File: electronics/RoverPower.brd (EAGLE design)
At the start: 31.8 x 31.8 mm, 13 parts, among them U1 LM2940

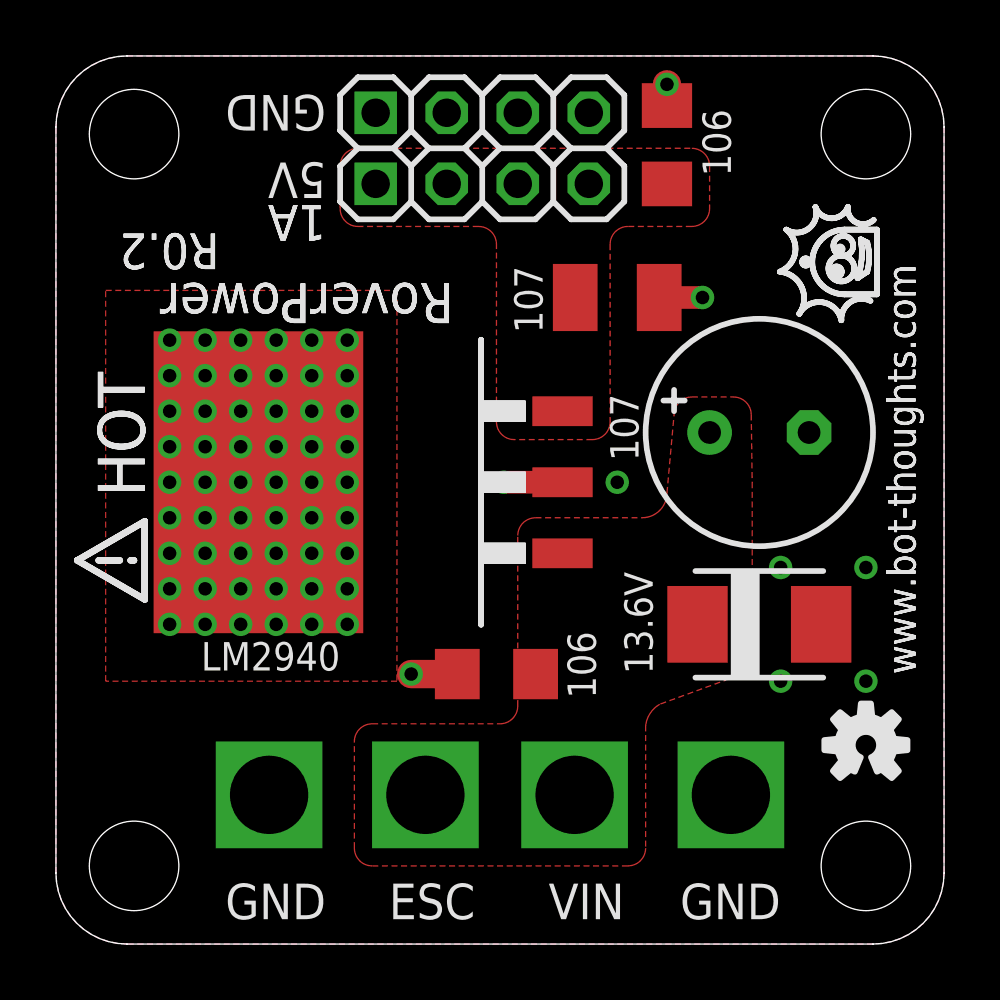
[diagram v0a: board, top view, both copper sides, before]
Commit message: copied power polygons to bottom layer, added vias. Changed capacitor to smaller version, revised TVS to higher voltage, changed layout.
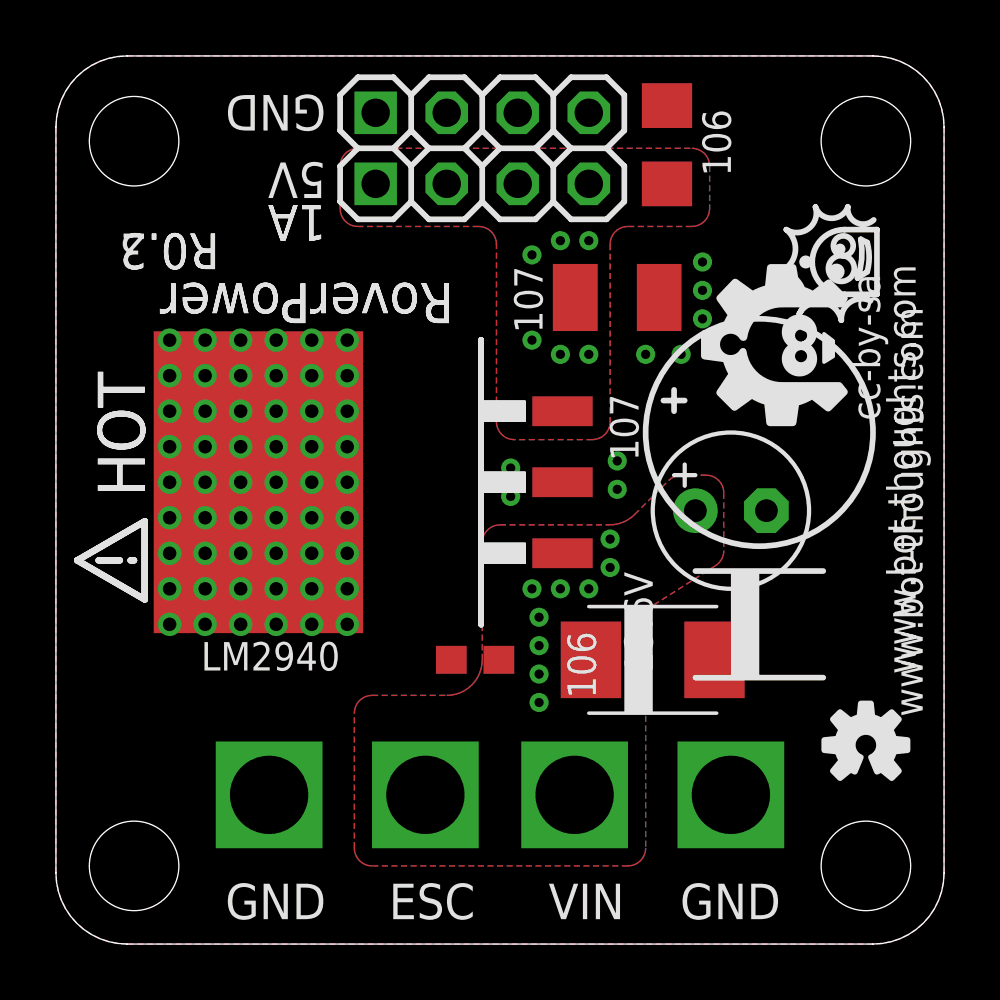
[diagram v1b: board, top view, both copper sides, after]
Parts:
- removed LOGO1: OSHW-LOGOS, SparkFun-Aesthetics:OSHW-LOGO-S
- added U$2: BTLOGO-LOGO-MD, bt:BTLOGOM
- C1: value 107 -> 476; device rcl:E3,5-8 -> rcl:E2,5-6
- C2: value 106 -> 104; device rcl:C1206 -> rcl:C0603
- D1: value 13.6V -> 25.5V
- moved D1 4.02 mm to (21.3, 10.2)
- moved C1 2.97 mm to (24.1, 15.5)
- moved C2 0.92 mm to (15.0, 10.2)
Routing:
- net GND: track 6.06 -> 0.00 mm
- added copper zone on layer 16, net 5V
- added copper zone on layer 16, net BAT+
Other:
- board text added: "R0.3"
- board text added: "cc-by-sa"

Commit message: Added more vias, changed output 10uf to .1uf
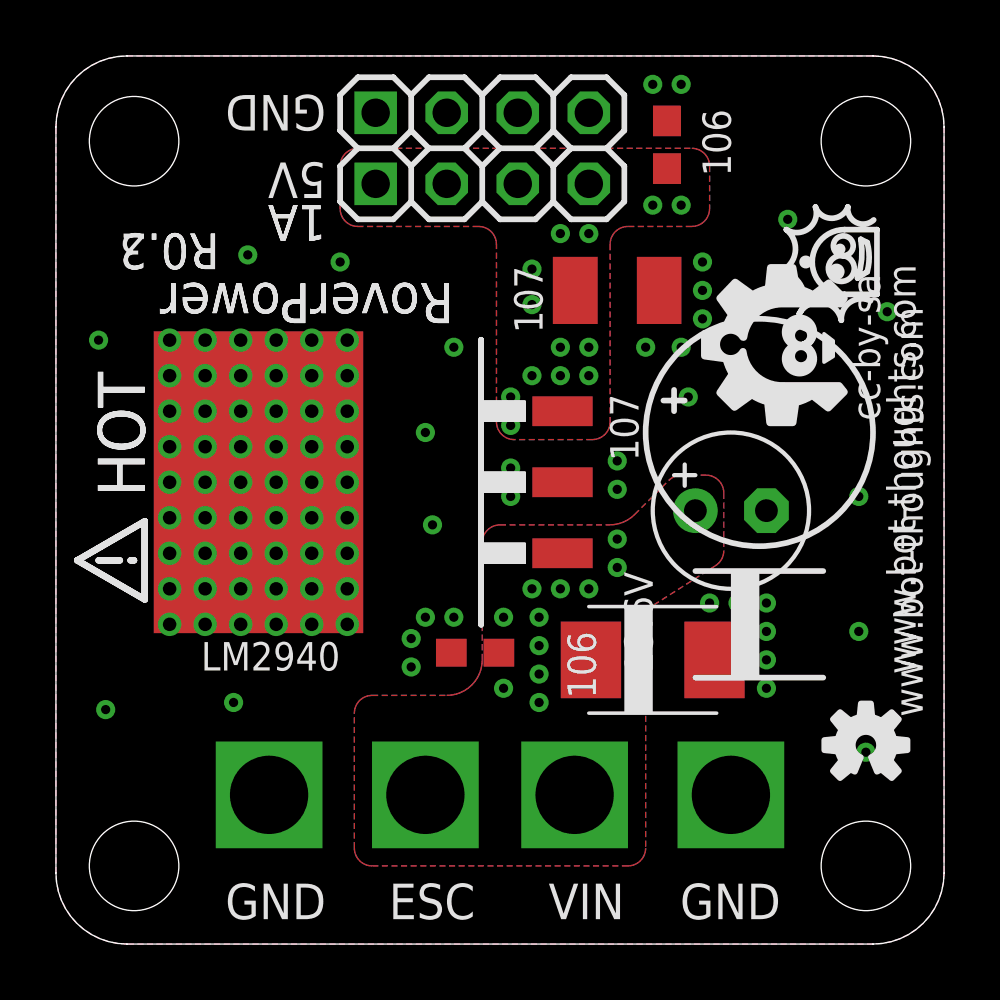
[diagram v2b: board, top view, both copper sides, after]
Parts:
- C3: value 106 -> 104; device rcl:C1206 -> rcl:C0603
- moved C2 0.25 mm to (15.0, 10.4)
- moved C4 0.25 mm to (20.1, 23.4)
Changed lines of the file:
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@@
 <attribute name="VALUE" x="25.908" y="2.159" size="1.27" layer="27" font="vector" ratio="12" rot="R180"/>
 </element>
-<element name="C3" library="rcl" package="C1206" value="106" x="21.844" y="28.575" smashed="yes" rot="R90">
+<element name="C3" library="rcl" package="C0603" value="104" x="21.844" y="28.575" smashed="yes" rot="R90">
 <attribute name="VOLTAGE" value="10V" x="21.844" y="28.575" size="1.778" layer="27" rot="R90" display="off"/>
-<attribute name="VALUE" x="23.114" y="29.845" size="1.016" layer="27" font="vector" ratio="12" rot="R270"/>
+<attribute name="VALUE" x="22.86" y="30.099" size="1.016" layer="27" font="vector" ratio="12" rot="R270"/>
 </element>
 <element name="D1" library="bt_diode" package="DO-214AA" value="25.5V" x="21.336" y="10.16" smashed="yes">
@@
 <attribute name="VALUE" x="10.16" y="10.795" size="1.016" layer="27" font="vector" ratio="12" rot="R180"/>
 </element>
-<element name="C4" library="rcl" package="SMC_B" value="107" x="20.066" y="23.114" smashed="yes">
-<attribute name="VOLTAGE" value="10V" x="20.066" y="23.114" size="1.778" layer="27" display="off"/>
-<attribute name="VALUE" x="17.399" y="21.844" size="1.016" layer="27" font="vector" ratio="12" rot="R90"/>
+<element name="C4" library="rcl" package="SMC_B" value="107" x="20.066" y="23.368" smashed="yes">
+<attribute name="VOLTAGE" value="10V" x="20.066" y="23.368" size="1.778" layer="27" display="off"/>
+<attribute name="VALUE" x="17.399" y="22.098" size="1.016" layer="27" font="vector" ratio="12" rot="R90"/>
 </element>
 <element name="JP5" library="bt_electromech" package="PAD_12GA" value="ESC" x="13.208" y="5.334" smashed="yes" rot="R90">
@@
 <attribute name="VALUE" x="25.781" y="12.319" size="1.016" layer="27" font="vector" ratio="12"/>
 </element>
-<element name="C2" library="rcl" package="C0603" value="104" x="14.986" y="10.16" smashed="yes" rot="R180">
-<attribute name="VOLTAGE" value="25V" x="14.986" y="10.16" size="1.778" layer="27" ratio="12" rot="R180" display="off"/>
-<attribute name="VALUE" x="16.383" y="9.271" size="1.016" layer="27" font="vector" ratio="12" rot="R180"/>
+<element name="C2" library="rcl" package="C0603" value="104" x="14.986" y="10.414" smashed="yes" rot="R180">
+<attribute name="VOLTAGE" value="25V" x="14.986" y="10.414" size="1.778" layer="27" ratio="12" rot="R180" display="off"/>
+<attribute name="VALUE" x="16.129" y="9.525" size="1.016" layer="27" font="vector" ratio="12" rot="R180"/>
 </element>
 </elements>
@@
 <vertex x="10.795" y="25.654" curve="-90"/>
 </polygon>
-<via x="19.05" y="21.082" extent="1-16" drill="0.3302"/>
-<via x="18.034" y="21.082" extent="1-16" drill="0.3302"/>
-<via x="17.018" y="21.59" extent="1-16" drill="0.3302"/>
-<via x="17.018" y="24.638" extent="1-16" drill="0.3302"/>
-<via x="18.034" y="25.146" extent="1-16" drill="0.3302"/>
-<via x="19.05" y="25.146" extent="1-16" drill="0.3302"/>
+<via x="19.05" y="21.336" extent="1-16" drill="0.3302"/>
+<via x="18.034" y="21.336" extent="1-16" drill="0.3302"/>
+<via x="17.018" y="22.86" extent="1-16" drill="0.3302"/>
+<via x="17.018" y="24.13" extent="1-16" drill="0.3302"/>
+<via x="18.034" y="25.4" extent="1-16" drill="0.3302"/>
+<via x="19.05" y="25.4" extent="1-16" drill="0.3302"/>
+<via x="16.256" y="18.542" extent="1-16" drill="0.3302"/>
+<via x="16.256" y="19.558" extent="1-16" drill="0.3302"/>
+<via x="17.018" y="20.32" extent="1-16" drill="0.3302"/>
+<via x="18.034" y="20.32" extent="1-16" drill="0.3302"/>
+<via x="19.05" y="20.32" extent="1-16" drill="0.3302"/>
+<via x="21.336" y="26.416" extent="1-16" drill="0.3302"/>
+<via x="22.352" y="26.416" extent="1-16" drill="0.3302"/>
 </signal>
 <signal name="GND">
@@
 <via x="20.066" y="16.256" extent="1-16" drill="0.3302"/>
 <via x="20.066" y="17.272" extent="1-16" drill="0.3302"/>
-<via x="21.082" y="21.082" extent="1-16" drill="0.3302"/>
-<via x="22.352" y="21.082" extent="1-16" drill="0.3302"/>
+<via x="21.082" y="21.336" extent="1-16" drill="0.3302"/>
+<via x="22.352" y="21.336" extent="1-16" drill="0.3302"/>
 <via x="23.114" y="24.384" extent="1-16" drill="0.3302"/>
 <via x="23.114" y="23.368" extent="1-16" drill="0.3302"/>
@@
 <contactref element="C1" pad="-"/>
 <contactref element="C2" pad="2"/>
+<via x="14.224" y="11.684" extent="1-16" drill="0.3302"/>
+<via x="13.208" y="11.684" extent="1-16" drill="0.3302"/>
+<via x="12.7" y="10.922" extent="1-16" drill="0.3302"/>
+<via x="12.7" y="9.906" extent="1-16" drill="0.3302"/>
+<via x="23.368" y="12.192" extent="1-16" drill="0.3302"/>
+<via x="24.384" y="12.192" extent="1-16" drill="0.3302"/>
+<via x="25.4" y="12.192" extent="1-16" drill="0.3302"/>
+<via x="25.4" y="11.176" extent="1-16" drill="0.3302"/>
+<via x="25.4" y="10.16" extent="1-16" drill="0.3302"/>
+<via x="25.4" y="9.144" extent="1-16" drill="0.3302"/>
+<via x="13.462" y="14.986" extent="1-16" drill="0.3302"/>
+<via x="13.208" y="18.288" extent="1-16" drill="0.3302"/>
+<via x="14.224" y="21.336" extent="1-16" drill="0.3302"/>
+<via x="1.778" y="8.382" extent="1-16" drill="0.3302"/>
+<via x="6.35" y="8.636" extent="1-16" drill="0.3302"/>
+<via x="28.702" y="16.002" extent="1-16" drill="0.3302"/>
+<via x="26.162" y="25.908" extent="1-16" drill="0.3302"/>
+<via x="22.606" y="19.558" extent="1-16" drill="0.3302"/>
+<via x="28.702" y="11.176" extent="1-16" drill="0.3302"/>
+<via x="6.858" y="24.638" extent="1-16" drill="0.3302"/>
+<via x="1.524" y="21.59" extent="1-16" drill="0.3302"/>
+<via x="10.16" y="24.384" extent="1-16" drill="0.3302"/>
+<via x="29.718" y="22.606" extent="1-16" drill="0.3302"/>
+<via x="28.956" y="6.858" extent="1-16" drill="0.3302"/>
+<via x="22.352" y="30.734" extent="1-16" drill="0.3302"/>
+<via x="21.336" y="30.734" extent="1-16" drill="0.3302"/>
 </signal>
 <signal name="BAT+">
@@
 <vertex x="15.24" y="14.351" curve="-90"/>
 </polygon>
-<via x="19.812" y="14.478" extent="1-16" drill="0.3302"/>
-<via x="19.812" y="13.462" extent="1-16" drill="0.3302"/>
+<via x="20.066" y="14.478" extent="1-16" drill="0.3302"/>
+<via x="20.066" y="13.462" extent="1-16" drill="0.3302"/>
 <via x="19.05" y="12.7" extent="1-16" drill="0.3302"/>
 <via x="18.034" y="12.7" extent="1-16" drill="0.3302"/>
@@
 <via x="17.272" y="8.636" extent="1-16" drill="0.3302"/>
 <contactref element="C2" pad="1"/>
+<via x="16.002" y="11.684" extent="1-16" drill="0.3302"/>
+<via x="16.002" y="9.144" extent="1-16" drill="0.3302"/>
 </signal>
 </signals>
